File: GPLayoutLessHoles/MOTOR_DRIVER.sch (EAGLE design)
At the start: 93 parts, among them T1 2N2222, T2 2N2222, U7 ATMEGA328P_TQFP, Y1 16MHz

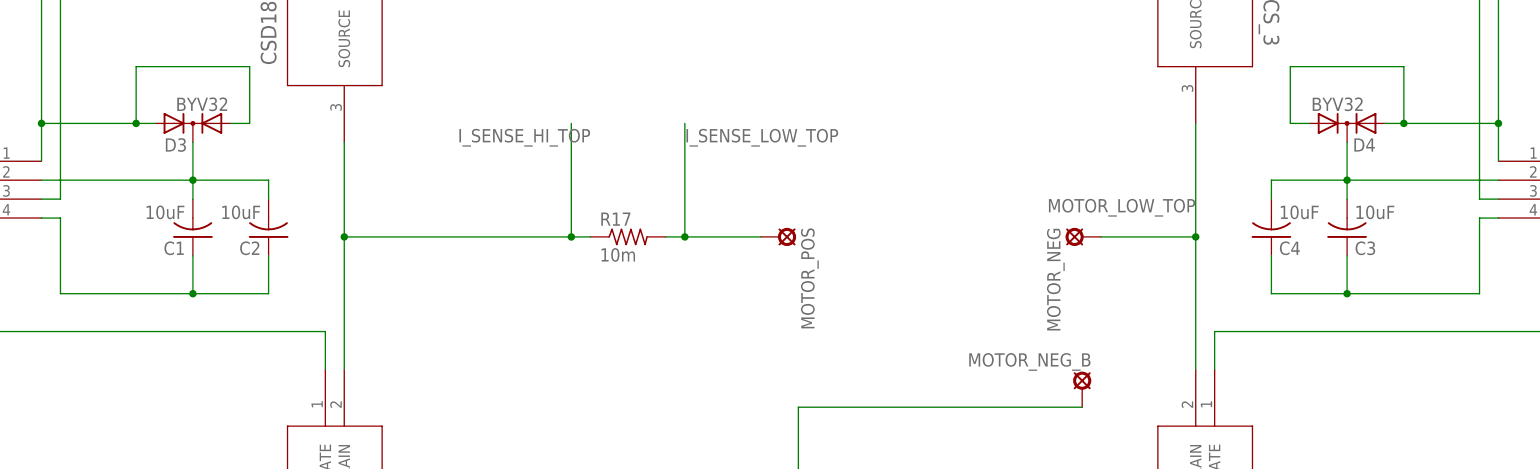
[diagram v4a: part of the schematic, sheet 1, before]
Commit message: new caps rerouted a lot, thinner wires, wider clearances
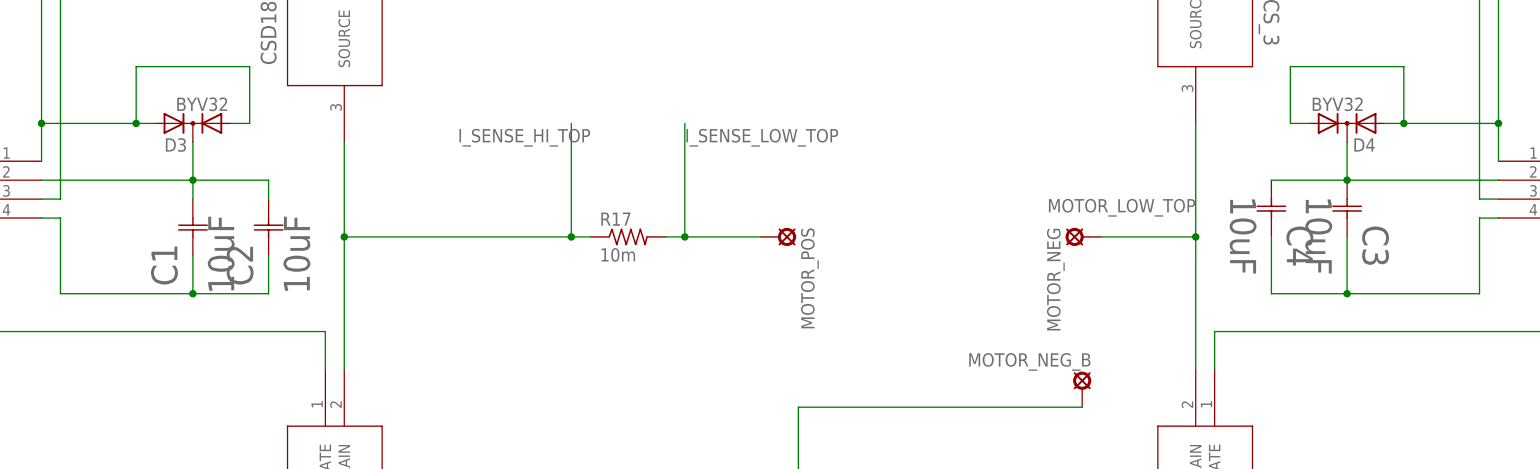
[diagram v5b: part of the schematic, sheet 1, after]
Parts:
- C1, C2, C3, C4: device resistor:C-US025-050X050 -> cap-aluminum:EEE1VA100WR
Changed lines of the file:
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@@
 <part name="FRAME1" library="frames" deviceset="A3L-LOC" device=""/>
 <part name="GATE1" library="MIC4604" deviceset="MIC4604YM" device=""/>
-<part name="C1" library="resistor" deviceset="C-US" device="025-050X050" value="10uF"/>
-<part name="C2" library="resistor" deviceset="C-US" device="025-050X050" value="10uF"/>
+<part name="C1" library="cap-aluminum" deviceset="EEE1VA100WR" device="" value="10uF"/>
+<part name="C2" library="cap-aluminum" deviceset="EEE1VA100WR" device="" value="10uF"/>
 <part name="MOTOR_POS" library="solpad" deviceset="SE14" device=""/>
 <part name="TOP_REV" library="CSD18502KCS" deviceset="CSD18502KCS_KCS_3" device=""/>
 <part name="BOT_FWD" library="CSD18502KCS" deviceset="CSD18502KCS_KCS_3" device=""/>
 <part name="GATE2" library="MIC4604" deviceset="MIC4604YM" device=""/>
-<part name="C3" library="resistor" deviceset="C-US" device="025-050X050" value="10uF"/>
-<part name="C4" library="resistor" deviceset="C-US" device="025-050X050" value="10uF"/>
+<part name="C3" library="cap-aluminum" deviceset="EEE1VA100WR" device="" value="10uF"/>
+<part name="C4" library="cap-aluminum" deviceset="EEE1VA100WR" device="" value="10uF"/>
 <part name="MOTOR_NEG" library="solpad" deviceset="SE14" device=""/>
 <part name="FRAME2" library="frames" deviceset="A3L-LOC" device=""/>
@@
 <instance part="FRAME1" gate="G$1" x="0" y="0"/>
 <instance part="GATE1" gate="A" x="86.36" y="142.24" rot="MR0"/>
-<instance part="C1" gate="G$1" x="106.68" y="132.08" rot="R180"/>
-<instance part="C2" gate="G$1" x="116.84" y="132.08" rot="R180"/>
+<instance part="C1" gate="A" x="106.68" y="129.54" rot="R90"/>
+<instance part="C2" gate="A" x="116.84" y="129.54" rot="R90"/>
 <instance part="MOTOR_POS" gate="1" x="185.42" y="132.08" rot="R270"/>
 <instance part="TOP_REV" gate="A" x="243.84" y="213.36" rot="R270"/>
 <instance part="BOT_FWD" gate="A" x="243.84" y="114.3" rot="R270"/>
 <instance part="GATE2" gate="A" x="281.94" y="142.24"/>
-<instance part="C3" gate="G$1" x="261.62" y="132.08" rot="MR180"/>
-<instance part="C4" gate="G$1" x="251.46" y="132.08" rot="MR180"/>
+<instance part="C3" gate="A" x="261.62" y="132.08" rot="MR90"/>
+<instance part="C4" gate="A" x="251.46" y="132.08" rot="MR90"/>
 <instance part="MOTOR_NEG" gate="1" x="226.06" y="132.08" rot="MR270"/>
 <instance part="D3" gate="1" x="106.68" y="147.32" rot="R180"/>
@@
 <wire x1="86.36" y1="134.62" x2="88.9" y2="134.62" width="0.1524" layer="91"/>
 <wire x1="88.9" y1="134.62" x2="88.9" y2="124.46" width="0.1524" layer="91"/>
-<pinref part="C2" gate="G$1" pin="1"/>
+<pinref part="C2" gate="A" pin="1"/>
 <wire x1="88.9" y1="124.46" x2="106.68" y2="124.46" width="0.1524" layer="91"/>
 <wire x1="106.68" y1="124.46" x2="116.84" y2="124.46" width="0.1524" layer="91"/>
 <wire x1="116.84" y1="124.46" x2="116.84" y2="129.54" width="0.1524" layer="91"/>
-<pinref part="C1" gate="G$1" pin="1"/>
+<pinref part="C1" gate="A" pin="1"/>
 <wire x1="106.68" y1="129.54" x2="106.68" y2="124.46" width="0.1524" layer="91"/>
 <junction x="106.68" y="124.46"/>
@@
 <segment>
 <pinref part="GATE1" gate="A" pin="HB"/>
-<pinref part="C2" gate="G$1" pin="2"/>
+<pinref part="C2" gate="A" pin="2"/>
 <wire x1="86.36" y1="139.7" x2="106.68" y2="139.7" width="0.1524" layer="91"/>
 <wire x1="106.68" y1="139.7" x2="116.84" y2="139.7" width="0.1524" layer="91"/>
 <wire x1="116.84" y1="139.7" x2="116.84" y2="137.16" width="0.1524" layer="91"/>
-<pinref part="C1" gate="G$1" pin="2"/>
+<pinref part="C1" gate="A" pin="2"/>
 <wire x1="106.68" y1="137.16" x2="106.68" y2="139.7" width="0.1524" layer="91"/>
 <junction x="106.68" y="139.7"/>
@@
 <wire x1="281.94" y1="134.62" x2="279.4" y2="134.62" width="0.1524" layer="91"/>
 <wire x1="279.4" y1="134.62" x2="279.4" y2="124.46" width="0.1524" layer="91"/>
-<pinref part="C4" gate="G$1" pin="1"/>
+<pinref part="C4" gate="A" pin="1"/>
 <wire x1="279.4" y1="124.46" x2="261.62" y2="124.46" width="0.1524" layer="91"/>
 <wire x1="261.62" y1="124.46" x2="251.46" y2="124.46" width="0.1524" layer="91"/>
-<wire x1="251.46" y1="124.46" x2="251.46" y2="129.54" width="0.1524" layer="91"/>
-<pinref part="C3" gate="G$1" pin="1"/>
-<wire x1="261.62" y1="129.54" x2="261.62" y2="124.46" width="0.1524" layer="91"/>
+<wire x1="251.46" y1="124.46" x2="251.46" y2="132.08" width="0.1524" layer="91"/>
+<pinref part="C3" gate="A" pin="1"/>
+<wire x1="261.62" y1="132.08" x2="261.62" y2="124.46" width="0.1524" layer="91"/>
 <junction x="261.62" y="124.46"/>
 </segment>
@@
 <segment>
 <pinref part="GATE2" gate="A" pin="HB"/>
-<pinref part="C4" gate="G$1" pin="2"/>
+<pinref part="C4" gate="A" pin="2"/>
 <wire x1="281.94" y1="139.7" x2="261.62" y2="139.7" width="0.1524" layer="91"/>
 <wire x1="261.62" y1="139.7" x2="251.46" y2="139.7" width="0.1524" layer="91"/>
-<wire x1="251.46" y1="139.7" x2="251.46" y2="137.16" width="0.1524" layer="91"/>
-<pinref part="C3" gate="G$1" pin="2"/>
-<wire x1="261.62" y1="137.16" x2="261.62" y2="139.7" width="0.1524" layer="91"/>
+<pinref part="C3" gate="A" pin="2"/>
 <junction x="261.62" y="139.7"/>
 <pinref part="D4" gate="1" pin="C"/>
